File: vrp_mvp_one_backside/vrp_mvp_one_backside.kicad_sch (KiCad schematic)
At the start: 7 parts, among them J2 BACKSIDE_INTERFACE, J7 BACKSIDE_INTERFACE_2, Q2 MMBT2222A

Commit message: minor changes
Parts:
- added H1, H2, H3, H4: MountingHole_Pad, MountingHole:MountingHole_2.7mm_M2.5_DIN965_Pad, symbol Mechanical:MountingHole_Pad
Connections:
- net GND: now also H1.1, H2.1, H3.1, H4.1

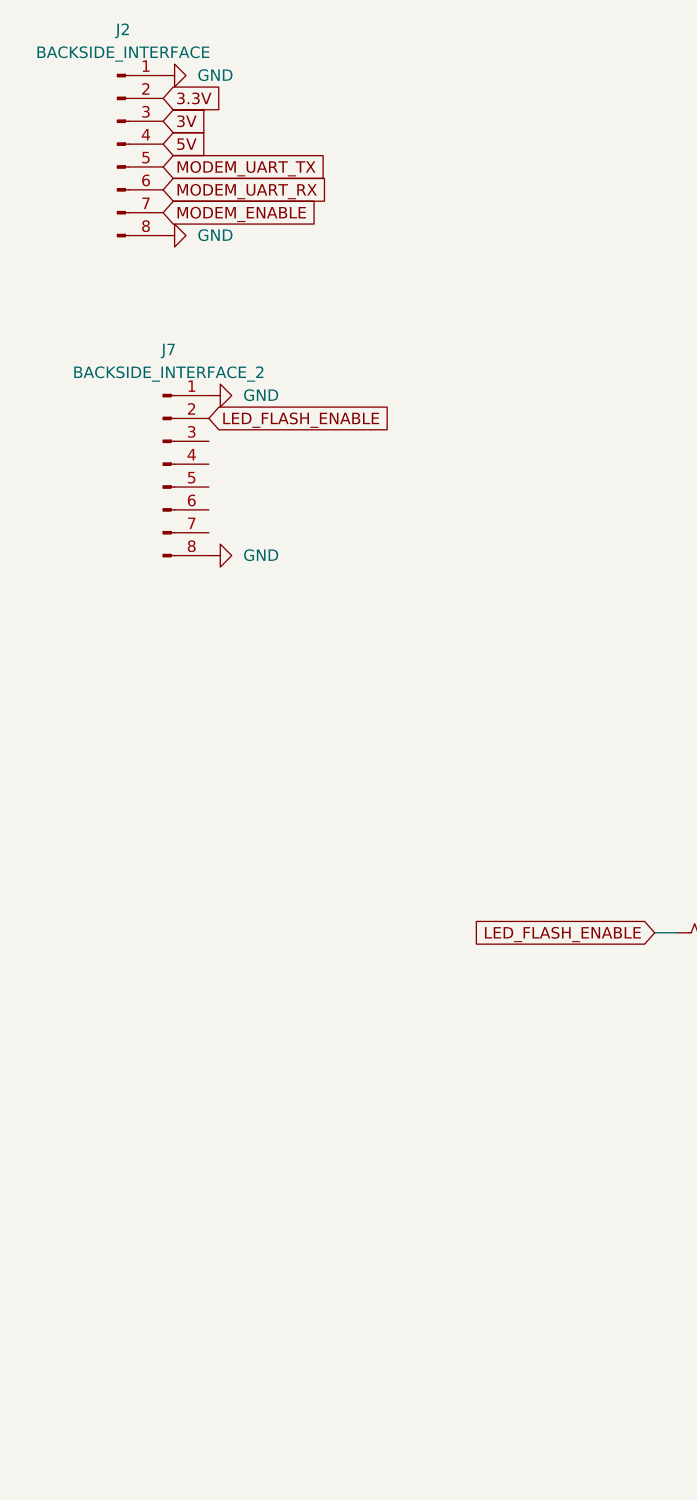
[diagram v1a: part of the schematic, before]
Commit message: audio, more routing, switched to lipo battery
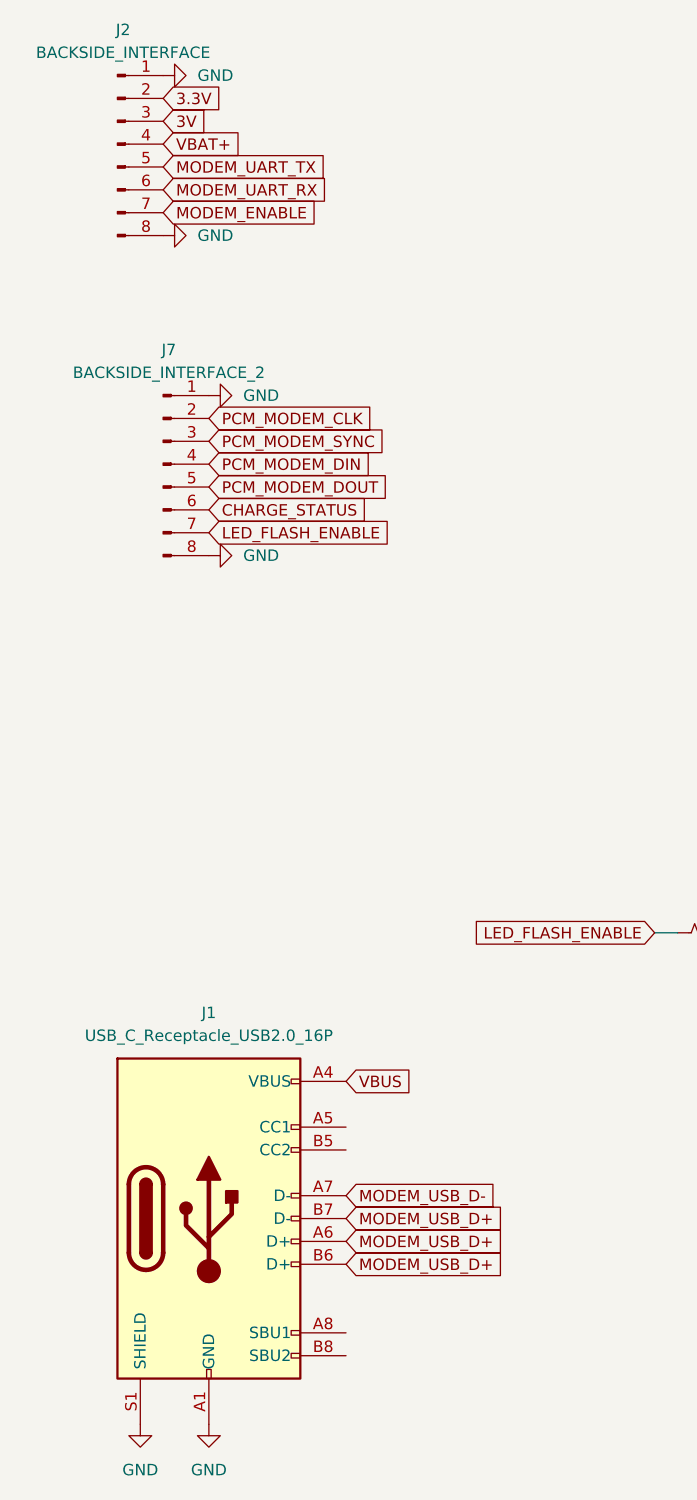
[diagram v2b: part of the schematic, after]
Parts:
- added J1: USB_C_Receptacle_USB2.0_16P, Connector_USB:USB_C_Receptacle_GCT_USB4105-xx-A_16P_TopMnt_Horizontal, symbol Connector:USB_C_Receptacle_USB2.0_16P
- R11, R12, R13: footprint (none) -> Resistor_SMD:R_0805_2012Metric_Pad1.20x1.40mm_HandSolder
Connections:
- net GND: now also J1.A1 (GND), J1.A12 (GND), J1.B1 (GND), J1.B12 (GND), J1.S1 (SHIELD)
- net LED_FLASH_ENABLE: now also J7.7 (Pin_7); no longer J7.2 (Pin_2)
- net PCM_MODEM_SYNC: now reaches J7.3 (Pin_3)
- net PCM_MODEM_DIN: now reaches J7.4 (Pin_4)
- net PCM_MODEM_DOUT: now reaches J7.5 (Pin_5)
- net CHARGE_STATUS: now reaches J7.6 (Pin_6)
- net 5V renamed VBAT+
- new net MODEM_USB_D+: J1.A6 (D+), J1.B6 (D+), J1.B7 (D-)
- new net MODEM_USB_D-: J1.A7 (D-)
- new net PCM_MODEM_CLK: J7.2 (Pin_2)
- new net VBUS: J1.A4 (VBUS), J1.A9 (VBUS), J1.B4 (VBUS), J1.B9 (VBUS)

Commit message: more routing and part placement
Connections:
- net MODEM_UART_RX renamed UART_MODEM_RX
- net MODEM_UART_TX renamed UART_MODEM_TX
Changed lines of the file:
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@@
 		)
 	)
-	(global_label "MODEM_UART_TX"
+	(global_label "UART_MODEM_TX"
 		(shape input)
 		(at 36.83 38.1 0)
@@
 		)
 	)
-	(global_label "MODEM_UART_RX"
+	(global_label "UART_MODEM_RX"
 		(shape input)
 		(at 36.83 40.64 0)

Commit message: changes
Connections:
- net MODEM_USB_D+: no longer J1.B7 (D-)
- net MODEM_USB_D-: now also J1.B7 (D-)
- net PCM_MODEM_DOUT: now also J7.3 (Pin_3); no longer J7.5 (Pin_5)
- net PCM_MODEM_SYNC: now also J7.5 (Pin_5); no longer J7.3 (Pin_3)
- net UART_MODEM_RX: now also J2.5 (Pin_5); no longer J2.6 (Pin_6)
- net UART_MODEM_TX: now also J2.6 (Pin_6); no longer J2.5 (Pin_5)
